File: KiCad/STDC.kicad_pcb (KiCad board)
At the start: 4 copper layers, 38 x 48 mm, 0 parts

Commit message: Use JLCPCB setup ported from Altium
https://gitlab.ethz.ch/villanif/altium_files/-/tree/master/example_design_rules
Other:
- rule pad_to_mask_clearance: 0 -> 0.075
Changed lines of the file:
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@@
 			(dielectric_constraints no)
 		)
-		(pad_to_mask_clearance 0)
+		(pad_to_mask_clearance 0.075)
 		(allow_soldermask_bridges_in_footprints no)
 		(tenting front back)

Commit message: First Draft PCB Layout
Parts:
- added C1: 4u7, Capacitor_SMD:C_0402_1005Metric, F.Cu at (149.1, 116.0)
- added C10: 15pF, Capacitor_SMD:C_0402_1005Metric, F.Cu at (137.8, 125.3)
- added C11: 100n, Capacitor_SMD:C_0402_1005Metric, F.Cu at (149.7, 103.3)
- added C12: 100n, Capacitor_SMD:C_0402_1005Metric, F.Cu at (135.8, 111.2)
- added C13: 100n, Capacitor_SMD:C_0402_1005Metric, F.Cu at (133.9, 118.1)
- added C14: 100n, Capacitor_SMD:C_0402_1005Metric, F.Cu at (136.6, 119.2)
- added C15: 100n, Capacitor_SMD:C_0402_1005Metric, F.Cu at (132.5, 126.8)
- added C16: 100n, Capacitor_SMD:C_0402_1005Metric, F.Cu at (126.1, 120.4)
- added C17: 100n, Capacitor_SMD:C_0402_1005Metric, F.Cu at (126.3, 118.6)
- added C18: 4u7, Capacitor_SMD:C_0402_1005Metric, F.Cu at (143.3, 109.3)
- added C19: 470n, Capacitor_SMD:C_0402_1005Metric, F.Cu at (138.9, 106.1)
- added C2: 4u7, Capacitor_SMD:C_0402_1005Metric, F.Cu at (149.1, 117.0)
- added C20: 22n, Capacitor_SMD:C_0402_1005Metric, F.Cu at (138.9, 107.1)
- added C21: 10n, Capacitor_SMD:C_0402_1005Metric, F.Cu at (138.9, 105.1)
- added C22: 220n, Capacitor_SMD:C_0402_1005Metric, F.Cu at (138.5, 104.1)
- added C23: 2n2, Capacitor_SMD:C_0402_1005Metric, F.Cu at (144.2, 101.4)
- added C24: 100p, Capacitor_SMD:C_0402_1005Metric, F.Cu at (144.2, 102.4)
- added C25: 10n, Capacitor_SMD:C_0402_1005Metric, F.Cu at (145.8, 104.4)
- added C26: 22n, Capacitor_SMD:C_0402_1005Metric, F.Cu at (145.8, 106.5)
- added C27: 470n, Capacitor_SMD:C_0402_1005Metric, F.Cu at (145.8, 105.4)
- added C28: 10u, Capacitor_SMD:C_0402_1005Metric, F.Cu at (147.7, 110.0)
- added C29: 10u, Capacitor_SMD:C_0402_1005Metric, F.Cu at (147.7, 111.1)
- added C3: 1u, Capacitor_SMD:C_0402_1005Metric, F.Cu at (137.3, 128.7)
- added C30: 100p, Capacitor_SMD:C_0402_1005Metric, F.Cu at (147.7, 112.2)
- added C31: 4u7, Capacitor_SMD:C_0402_1005Metric, F.Cu at (141.3, 111.8)
- added C32: 4u7, Capacitor_SMD:C_0402_1005Metric, F.Cu at (143.5, 116.7)
- added C33: 10u, Capacitor_SMD:C_0402_1005Metric, F.Cu at (143.5, 117.8)
- added C34: 10u, Capacitor_SMD:C_0402_1005Metric, F.Cu at (141.3, 110.8)
- added C35: 100p, Capacitor_SMD:C_0402_1005Metric, F.Cu at (128.7, 138.3)
- added C36: 10u, Capacitor_SMD:C_0402_1005Metric, F.Cu at (136.9, 135.0)
- added C37: 100n, Capacitor_SMD:C_0402_1005Metric, F.Cu at (133.5, 142.8)
- added C38: 1u, Capacitor_SMD:C_0402_1005Metric, F.Cu at (133.6, 139.8)
- added C39: 1u, Capacitor_SMD:C_0402_1005Metric, F.Cu at (133.4, 140.8)
- added C4: 10n, Capacitor_SMD:C_0402_1005Metric, F.Cu at (138.3, 128.7)
- added C40: 10u, Capacitor_SMD:C_0402_1005Metric, F.Cu at (133.5, 141.8)
- added C41: 1u, Capacitor_SMD:C_0402_1005Metric, F.Cu at (132.2, 132.7)
- added C42: 22u, Capacitor_SMD:C_0402_1005Metric, F.Cu at (132.2, 133.8)
- added C43: 100n, Capacitor_SMD:C_0402_1005Metric, F.Cu at (131.0, 142.7)
- added C44: 100n, Capacitor_SMD:C_0402_1005Metric, F.Cu at (136.3, 142.3)
- added C45: 100n, Capacitor_SMD:C_0402_1005Metric, F.Cu at (135.3, 142.3)
- added C46: 1u, Capacitor_SMD:C_0402_1005Metric, F.Cu at (135.6, 140.6)
- added C47: 4u7, Capacitor_SMD:C_0402_1005Metric, F.Cu at (128.5, 141.8)
- added C48: 4u7, Capacitor_SMD:C_0402_1005Metric, F.Cu at (130.0, 140.6)
- added C49: 100n, Capacitor_SMD:C_0402_1005Metric, F.Cu at (145.0, 142.8)
- added C5: 100n, Capacitor_SMD:C_0402_1005Metric, F.Cu at (142.1, 119.7)
- added C50: 100n, Capacitor_SMD:C_0402_1005Metric, F.Cu at (128.7, 142.8)
- added C51: 100n, Capacitor_SMD:C_0402_1005Metric, F.Cu at (153.8, 109.3)
- added C52: 100n, Capacitor_SMD:C_0402_1005Metric, F.Cu at (159.3, 111.4)
- added C53: 100n, Capacitor_SMD:C_0402_1005Metric, F.Cu at (162.0, 104.5)
- added C54: 100n, Capacitor_SMD:C_0402_1005Metric, F.Cu at (159.8, 101.7)
- added C55: 100n, Capacitor_SMD:C_0402_1005Metric, F.Cu at (151.5, 105.8)
- added C56: 100n, Capacitor_SMD:C_0402_1005Metric, F.Cu at (142.8, 141.3)
- added C57: 100n, Capacitor_SMD:C_0402_1005Metric, F.Cu at (148.6, 135.3)
- added C58: 100n, Capacitor_SMD:C_0402_1005Metric, F.Cu at (154.8, 144.0)
- added C59: 100n, Capacitor_SMD:C_0402_1005Metric, F.Cu at (158.8, 147.1)
- added C6: 100n, Capacitor_SMD:C_0402_1005Metric, F.Cu at (142.1, 134.2)
- added C60: 100n, Capacitor_SMD:C_0402_1005Metric, F.Cu at (158.6, 125.2)
- added C7: 100n, Capacitor_SMD:C_0402_1005Metric, F.Cu at (149.2, 134.2)
- added C8: 100n, Capacitor_SMD:C_0402_1005Metric, F.Cu at (139.3, 121.8)
- added C9: 15pF, Capacitor_SMD:C_0402_1005Metric, F.Cu at (137.8, 123.3)
- added D1: Orange, LED_SMD:LED_0603_1608Metric, F.Cu at (136.6, 101.6)
- added D2: Red, LED_SMD:LED_0603_1608Metric, F.Cu at (161.8, 121.0)
- added D3: Blue, LED_SMD:LED_0603_1608Metric, F.Cu at (161.8, 117.9)
- added D4: Green, LED_SMD:LED_0603_1608Metric, F.Cu at (153.1, 146.7)
- added IC1: BQ26221PW, TI-BQ26221PW:SOP65P640X120-8N, F.Cu at (130.9, 121.0)
- added IC2: R1200N001A-TR-FE, LIB_R1200N001A-TR-FE:SOT95P280X110-6N, F.Cu at (129.0, 133.8)
- added IC3: MS5849-30BA, MS5849-30BA:MS584930BA, F.Cu at (158.7, 104.9)
- added IC4: W25Q32JWSNIQ, Winbond-W25Q32JWSNIQ:SOIC127P600X175-8N, F.Cu at (156.3, 128.5)
- added J1: TC2030, Connector:Tag-Connect_TC2030-IDC-NL_2x03_P1.27mm_Vertical, F.Cu at (155.6, 115.2)
- added J2: Conn_01x03_BATT, Connector_JST:JST_PH_S3B-PH-K_1x03_P2.00mm_Horizontal, F.Cu at (128.2, 102.5)
- added J3: Conn_01x34_NHD_18, Connector_FFC-FPC:TE_3-1734839-4_1x34-1MP_P0.5mm_Horizontal, F.Cu at (137.5, 145.8)
- added L1: WPC Charging RX, L_IWAS4832-QiCoil:L_IWAS4832ABEB110JF1, F.Cu at (143.0, 103.3)
- added L2: 4u7, Inductor_SMD:L_1210_3225Metric, F.Cu at (138.5, 112.5)
- added L3: 2u2, Inductor_SMD:L_1210_3225Metric, F.Cu at (146.5, 115.2)
- added L4: 10u, Inductor_SMD:L_1812_4532Metric, F.Cu at (129.4, 130.0)
- added Q1: AO3400A, Package_TO_SOT_SMD:SOT-23, F.Cu at (127.5, 111.4)
- added Q2: AO3400A, Package_TO_SOT_SMD:SOT-23, F.Cu at (127.5, 115.4)
- added Q3: DMG2302U, Package_TO_SOT_SMD:SOT-23, F.Cu at (139.3, 134.7)
- added Q4: DMG2302U, Package_TO_SOT_SMD:SOT-23, F.Cu at (134.5, 130.6)
- added R1: 10k, Resistor_SMD:R_0402_1005Metric, F.Cu at (137.0, 126.9)
- added R10: 100k, Resistor_SMD:R_0402_1005Metric, F.Cu at (137.7, 119.2)
- added R11: 20m, Resistor_SMD:R_0402_1005Metric, F.Cu at (137.2, 117.7)
- added R12: 680R, Resistor_SMD:R_0402_1005Metric, F.Cu at (135.8, 108.5)
- added R13: 150R, Resistor_SMD:R_0402_1005Metric, F.Cu at (145.7, 107.8)
- added R14: 220R, Resistor_SMD:R_0402_1005Metric, F.Cu at (147.7, 108.9)
- added R15: 2k2, Resistor_SMD:R_0402_1005Metric, F.Cu at (141.4, 109.3)
- added R16: 680R, Resistor_SMD:R_0402_1005Metric, F.Cu at (159.5, 120.1)
- added R17: 150R, Resistor_SMD:R_0402_1005Metric, F.Cu at (159.5, 118.9)
- added R18: 100k, Resistor_SMD:R_0402_1005Metric, F.Cu at (128.2, 136.8)
- added R19: 200k, Resistor_SMD:R_0402_1005Metric, F.Cu at (129.3, 136.8)
- added R2: 10k, Resistor_SMD:R_0402_1005Metric, F.Cu at (143.9, 119.3)
- added R20: 220k, Resistor_SMD:R_0402_1005Metric, F.Cu at (132.2, 134.9)
- added R21: 15k, Resistor_SMD:R_0402_1005Metric, F.Cu at (126.3, 134.0)
- added R22: 49.9R, Resistor_SMD:R_0402_1005Metric, F.Cu at (131.7, 139.2)
- added R23: 10k, Resistor_SMD:R_0402_1005Metric, F.Cu at (138.7, 140.0)
- added R24: 10k, Resistor_SMD:R_0402_1005Metric, F.Cu at (139.2, 138.6)
- added R25: 1M5, Resistor_SMD:R_0402_1005Metric, F.Cu at (143.0, 142.8)
- added R26: 2k2, Resistor_SMD:R_0402_1005Metric, F.Cu at (159.2, 108.5)
- added R27: 2k2, Resistor_SMD:R_0402_1005Metric, F.Cu at (161.1, 108.5)
- added R28: 2k2, Resistor_SMD:R_0402_1005Metric, F.Cu at (159.1, 112.8)
- added R29: 2k2, Resistor_SMD:R_0402_1005Metric, F.Cu at (159.1, 114.2)
- added R3: 150R, Resistor_SMD:R_0402_1005Metric, F.Cu at (134.8, 114.6)
- added R30: 10k, Resistor_SMD:R_0402_1005Metric, F.Cu at (149.7, 139.0)
- added R31: 10k, Resistor_SMD:R_0402_1005Metric, F.Cu at (149.8, 144.9)
- added R32: 10k, Resistor_SMD:R_0402_1005Metric, F.Cu at (151.3, 145.4)
- added R33: 680R, Resistor_SMD:R_0402_1005Metric, F.Cu at (154.5, 147.1)
- added R34: 10k, Resistor_SMD:R_0402_1005Metric, F.Cu at (152.1, 131.9)
- added R35: 10k, Resistor_SMD:R_0402_1005Metric, F.Cu at (160.7, 127.0)
- added R36: 10k, Resistor_SMD:R_0402_1005Metric, F.Cu at (161.2, 129.2)
- added R4: 10k, Resistor_SMD:R_0402_1005Metric, F.Cu at (127.2, 126.7)
- added R5: 10k, Resistor_SMD:R_0402_1005Metric, F.Cu at (132.7, 124.8)
- added R6: 10k, Resistor_SMD:R_0402_1005Metric, F.Cu at (127.6, 123.4)
- added R7: 1k, Resistor_SMD:R_0402_1005Metric, F.Cu at (130.4, 112.4)
- added R8: 10k, Resistor_SMD:R_0402_1005Metric, F.Cu at (131.1, 118.4)
- added R9: 100k, Resistor_SMD:R_0402_1005Metric, F.Cu at (132.7, 118.1)
- added TP1: TestPoint, TestPoint:TestPoint_THTPad_1.0x1.0mm_Drill0.5mm, F.Cu at (149.0, 101.8)
- added TP2: UART_TX, TestPoint:TestPoint_THTPad_1.0x1.0mm_Drill0.5mm, F.Cu at (151.0, 101.8)
- added TP3: UART_RX, TestPoint:TestPoint_THTPad_1.0x1.0mm_Drill0.5mm, F.Cu at (153.0, 101.8)
- added TP4: TestPoint, TestPoint:TestPoint_THTPad_1.0x1.0mm_Drill0.5mm, F.Cu at (155.0, 101.8)
- added U1: STM32L476RGTx, Package_QFP:LQFP-64_10x10mm_P0.5mm, F.Cu at (145.6, 127.0)
- added U10: SN74LV1T34DCK, Package_TO_SOT_SMD:SOT-353_SC-70-5, F.Cu at (144.7, 139.2)
- added U11: SN74LV1T34DCK, Package_TO_SOT_SMD:SOT-353_SC-70-5, F.Cu at (145.7, 136.6)
- added U12: RN4871, RF_Module:Microchip_RN4871, F.Cu at (154.3, 138.1)
- added U13: LM810, Package_TO_SOT_SMD:SOT-23, F.Cu at (148.4, 141.3)
- added U14: SN74LV1T34DCK, Package_TO_SOT_SMD:SOT-353_SC-70-5, F.Cu at (158.3, 145.2)
- added U2: DW01A, Package_TO_SOT_SMD:SOT-23-6, F.Cu at (133.2, 111.9)
- added U3: TXS0101DBV, Package_TO_SOT_SMD:SOT-23-6, F.Cu at (129.8, 126.2)
- added U4: BQ51050BRHL, Package_DFN_QFN:Texas_VQFN-RHL-20, F.Cu at (142.5, 106.0)
- added U5: PAM2306AYPKE, Package_DFN_QFN:WDFN-12-1EP_3x3mm_P0.45mm_EP1.7x2.5mm, F.Cu at (142.3, 114.2)
- added U6: MCP1700x-250xxTT, Package_TO_SOT_SMD:SOT-23, F.Cu at (135.8, 136.9)
- added U7: SN74LV1T34DCK, Package_TO_SOT_SMD:SOT-353_SC-70-5, F.Cu at (155.7, 109.6)
- added U8: SN74LV1T34DCK, Package_TO_SOT_SMD:SOT-353_SC-70-5, F.Cu at (153.9, 105.5)
- added U9: PCA9306, Package_SON:X2SON-8_1.4x1mm_P0.35mm, F.Cu at (159.7, 109.9)
- added X1: Q13FC1350000400, Crystal:Crystal_SMD_3215-2Pin_3.2x1.5mm, F.Cu at (136.1, 124.3)
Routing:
- net DISPLAY_VCC: track 0.00 -> 19.9 mm
- net /Display/VCOMH: track 0.00 -> 16.9 mm
- added copper zone on B.Cu, net GND
- added copper zone on In1.Cu, net GND

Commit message: Implement Comments, Working on PCB Layout
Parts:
- removed the C15 at (132.5, 126.8)
- removed the C16 at (126.1, 120.4)
- removed the C17 at (126.3, 118.6)
- removed the C38 at (133.6, 139.8)
- removed Q3, Q4: DMG2302U, Package_TO_SOT_SMD:SOT-23
- removed the R10 at (137.7, 119.2)
- removed the R11 at (137.2, 117.7)
- removed the R4 at (127.2, 126.7)
- removed the R6 at (127.6, 123.4)
- removed the R8 at (131.1, 118.4)
- removed the R9 at (132.7, 118.1)
- added C37: 100n, Capacitor_SMD:C_0402_1005Metric, F.Cu at (137.5, 137.2)
- added D4: RB522ES-30T15R, RB522ES-30T15R:RB522ES30, F.Cu at (134.3, 135.0)
- added D5: RB522ES-30T15R, RB522ES-30T15R:RB522ES30, F.Cu at (132.5, 135.0)
- added IC2: TPS22916CNYFPR, TPS22916CNYFPR:BGA4C40P2X2_78X78X50, F.Cu at (133.8, 128.1)
- IC1: value BQ26221PW -> TPS22916CNYFPR; footprint TI-BQ26221PW:SOP65P640X120-8N -> TPS22916CNYFPR:BGA4C40P2X2_78X78X50
- U3: value TXS0101DBV -> MAX17262REWL_T; footprint Package_TO_SOT_SMD:SOT-23-6 -> MAX17262REWL_T:BGA9N40P3X3_144X146X69N
- moved IC1 16.1 mm to (140.2, 134.1)
- moved R28 9.98 mm to (158.8, 124.5)
- moved U3 7.63 mm to (132.3, 119.0), turned to 90 degrees
- moved R29 7.07 mm to (154.5, 130.4), turned to 90 degrees
- moved R30 6.84 mm to (154.4, 128.2), turned to -90 degrees
- moved C57 6.39 mm to (156.4, 131.2), turned to 0 degrees
- moved J2 6.17 mm to (132.0, 107.4), turned to 180 degrees
- moved J1 6.16 mm to (155.1, 121.4)
- moved R5 5.97 mm to (129.6, 119.7), turned to 0 degrees
- moved C30 5.05 mm to (148.5, 118.5), turned to 0 degrees
- moved R6 4.51 mm to (136.1, 104.0), turned to -90 degrees
- moved C38 4.04 mm to (136.0, 137.7), turned to 90 degrees
- moved C13 3.85 mm to (130.1, 118.2), turned to -90 degrees
- moved C48 3.53 mm to (153.6, 112.8)
- moved U7 3.53 mm to (155.4, 113.1)
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- renumbered C18 to C15, C19 to C16, C20 to C17, C21 to C18, C22 to C19, C23 to C20, C24 to C21, C25 to C22, C26 to C23, C27 to C24, C28 to C25, C29 to C26, C30 to C27, C31 to C28, C32 to C29, C33 to C30, C34 to C31, C35 to C32, C41 to C33, C42 to C34, C36 to C35, C37 to C36, C39 to C38, C40 to C39, C43 to C40, C44 to C41, C45 to C42, C46 to C43, C47 to C44, C48 to C45, C49 to C46, C50 to C47, C51 to C48, C52 to C49, C53 to C50, C54 to C51, C55 to C52, C56 to C53, C57 to C54, C58 to C55, C59 to C56, C60 to C57, D4 to D6, IC2 to IC3, IC3 to IC4, IC4 to IC5, R16 to R10, R17 to R11, R18 to R12, R19 to R13, R20 to R14, R21 to R15, R22 to R16, R23 to R17, R24 to R18, R25 to R19, R26 to R20, R27 to R21, R28 to R22, R29 to R23, R30 to R24, R31 to R25, R32 to R26, R33 to R27, R34 to R28, R35 to R29, R36 to R30, R7 to R4, R12 to R6, R13 to R7, R14 to R8, R15 to R9
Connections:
- C13 pad 1: /Power+Battery/BAT_STAT_SRP -> /Power+Battery/BATT+
- C13 pad 2: /Power+Battery/BATT- -> GND
- C14 pad 1: /Power+Battery/BAT_STAT_SRN -> /Power+Battery/Stat_REG
- C14 pad 2: /Power+Battery/BATT- -> GND
- C15 pad 1: BATTERY_PWR -> /Power+Battery/BATT+
- C28 pad 1: BATTERY_PWR -> SYS_PWR
- C29 pad 1: BATTERY_PWR -> SYS_PWR
- D1 pad 2: BATTERY_PWR -> /Power+Battery/BATT+
- J2 pad 3: BATTERY_PWR -> /Power+Battery/BATT+
- R3 pad 1: BATTERY_PWR -> /Power+Battery/BATT+
- R5 pad 1: +1V8 -> /Power+Battery/TS_CTRL
- R5 pad 2: /BAT_STATUS_HDQ -> /Power+Battery/TS_CTRL_R
- U1 pad 8: unconnected-(U1-PC0-Pad8) -> /Power+Battery/Batt_Status_SCL
- U1 pad 9: /BAT_STATUS_HDQ -> /Power+Battery/Batt_Status_SDA
- U4 pad 11: BATTERY_PWR -> /Power+Battery/BATT+
- U4 pad 4: BATTERY_PWR -> /Power+Battery/BATT+
- U5 pad 1: BATTERY_PWR -> SYS_PWR
- U5 pad 12: BATTERY_PWR -> SYS_PWR
- U5 pad 6: BATTERY_PWR -> SYS_PWR
- U5 pad 7: BATTERY_PWR -> SYS_PWR
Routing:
- net GND: track 0.00 -> 52.8 mm, vias 0 -> 45
- net +1V8: track 0.00 -> 46.5 mm
- net /Power+Battery/TS_CTRL: track 0.00 -> 42.0 mm, vias 0 -> 2
- net +3.3V: track 0.00 -> 27.0 mm
- net //Display_SPI_CS: track 0.00 -> 15.6 mm
- net /Power+Battery/Batt_Status_SDA: track 0.00 -> 13.6 mm, vias 0 -> 2
- net /Power+Battery/Batt_Status_SCL: track 0.00 -> 13.1 mm
- net /SPI_MISO: track 0.00 -> 12.1 mm
- net /SPI_NSS: track 0.00 -> 10.8 mm, vias 0 -> 2
- net /Power+Battery/AC1: track 0.00 -> 9.96 mm
- net /Power+Battery//CHARGE: track 0.00 -> 7.97 mm
- net /Display/VSL: track 0.00 -> 7.76 mm
- net DISPLAY_VCI: track 0.00 -> 7.69 mm
- net /Power+Battery/OC: track 0.00 -> 7.26 mm
- net DISPLAY_VCC: track 19.9 -> 26.8 mm
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- added copper zone on F.Cu, net /Display/17V_VFB
- added copper zone on F.Cu, net /Display/LX4
- added copper zone on F.Cu, net /Power+Battery/BATT+
- added copper zone on F.Cu, net /Power+Battery/FOD
- added copper zone on F.Cu, net DISPLAY_BATT_PWR
- added copper zone on F.Cu, net DISPLAY_VCC
- added copper zone on F.Cu, net DISPLAY_VCI
- added copper zone on F.Cu, net GND
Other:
- rule pad_to_mask_clearance: 0.075 -> 0.05

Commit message: PCB Layout V0.1 with errors
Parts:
- moved C2 11.7 mm to (137.4, 113.9), turned to -90 degrees
- moved C1 10.4 mm to (138.4, 113.9), turned to -90 degrees
- moved C30 6.25 mm to (142.6, 116.5), turned to 180 degrees
- moved D2 3.15 mm to (161.8, 117.8), turned to -90 degrees
- moved D3 3.09 mm to (161.8, 121.0), turned to 90 degrees
- moved C29 3.06 mm to (142.6, 115.3)
- moved C28 2.89 mm to (140.5, 110.6), turned to 0 degrees
- moved U5 2.61 mm to (141.6, 113.0)
- moved L2 2.38 mm to (137.6, 110.7)
- moved C31 2.30 mm to (140.5, 109.3)
- moved R28 1.29 mm to (160.1, 124.5)
- moved R10 1.20 mm to (159.9, 119.3)
- moved R11 1.15 mm to (159.9, 120.5)
- moved R29 0.72 mm to (154.0, 129.9), turned to 0 degrees
- moved L3 0.66 mm to (145.7, 115.5)
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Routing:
- net +1V8: track 46.5 -> 148.9 mm, vias 0 -> 5
- net +3.3V: track 27.0 -> 103.0 mm, vias 0 -> 3
- net /Power+Battery/BATT+: track 4.46 -> 60.6 mm, vias 0 -> 4
- net /Debug_UART_TX: track 0.00 -> 33.2 mm, vias 0 -> 1
- net /Debug_UART_RX: track 0.00 -> 32.9 mm, vias 0 -> 1
- net GND: track 52.8 -> 78.9 mm, vias 45 -> 87
- net /BLE_TX_IND: track 0.00 -> 25.7 mm, vias 0 -> 2
- net /Pressure Sensor/I2C_SDA: track 0.09 -> 23.2 mm, vias 0 -> 2
- net /Pressure Sensor/I2C_SCL: track 0.00 -> 21.6 mm, vias 0 -> 2
- net DISPLAY_EN: track 0.00 -> 18.7 mm, vias 0 -> 3
- net /Pressure Sensor/Pressure_INT: track 0.00 -> 18.5 mm, vias 0 -> 2
- net /Bluetooth Module/SYS_CONF: track 0.00 -> 18.2 mm
- net /DISPLAY_DATA_COMM: track 0.00 -> 17.2 mm, vias 0 -> 2
- net /DISPLAY_RST: track 0.00 -> 16.5 mm, vias 0 -> 2
- net /JTRST: track 0.00 -> 16.3 mm
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- added copper zone on F.Cu, net +1V8
- added copper zone on F.Cu, net +3.3V
- added copper zone on F.Cu, net /Power+Battery/AC2
- added copper zone on F.Cu, net /Power+Battery/BATT-
- added copper zone on F.Cu, net /Power+Battery/LX2
- added copper zone on F.Cu, net /Power+Battery/LX3
- added copper zone on F.Cu, net SYS_PWR
- added copper zone on In2.Cu, net SYS_PWR

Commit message: Fix almost all issues
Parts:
- moved R6 0.51 mm to (135.6, 104.1)
- moved R7 0.44 mm to (148.1, 108.3)
- moved C31 0.27 mm to (140.3, 109.5)
- moved C12 0.15 mm to (135.4, 112.5)
- moved C28 0.14 mm to (140.3, 110.6)
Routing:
- net /Power+Battery/BATT+: track 60.6 -> 9.06 mm, vias 4 -> 7
- net SYS_PWR: track 13.9 -> 1.13 mm, vias 8 -> 9
- net /Power+Battery//CHARGE: track 7.48 -> 8.70 mm, vias 2 -> 0
- net /Power+Battery/Batt_Status_SDA: track 13.9 -> 13.0 mm
- net +3.3V: track 103.0 -> 103.6 mm
- net /Power+Battery/Batt_Status_SCL: track 13.5 -> 13.1 mm, vias 2 -> 0
- net /Power+Battery/TS_CTRL: track 42.0 -> 42.3 mm, vias 2 -> 4
- added copper zone on In2.Cu, net /Power+Battery/BATT+

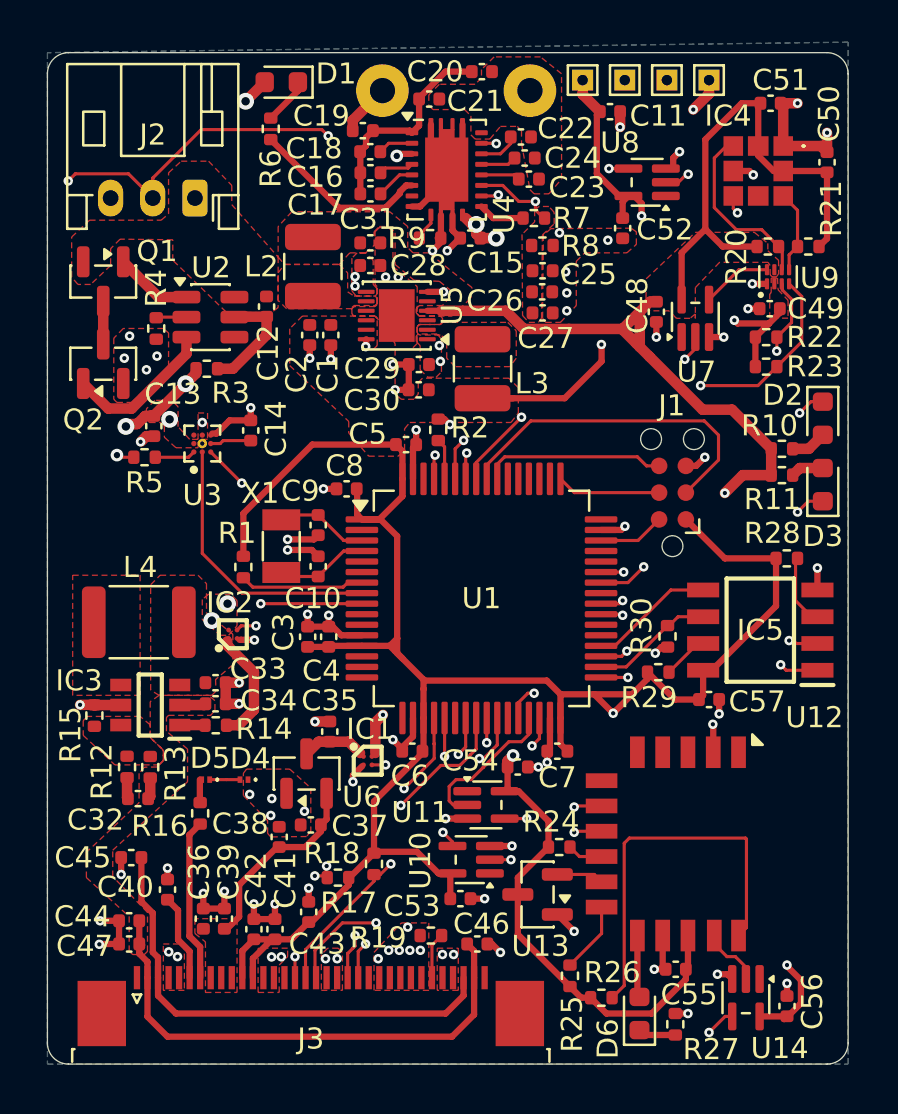
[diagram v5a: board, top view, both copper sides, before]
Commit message: Fix all except clearance violations
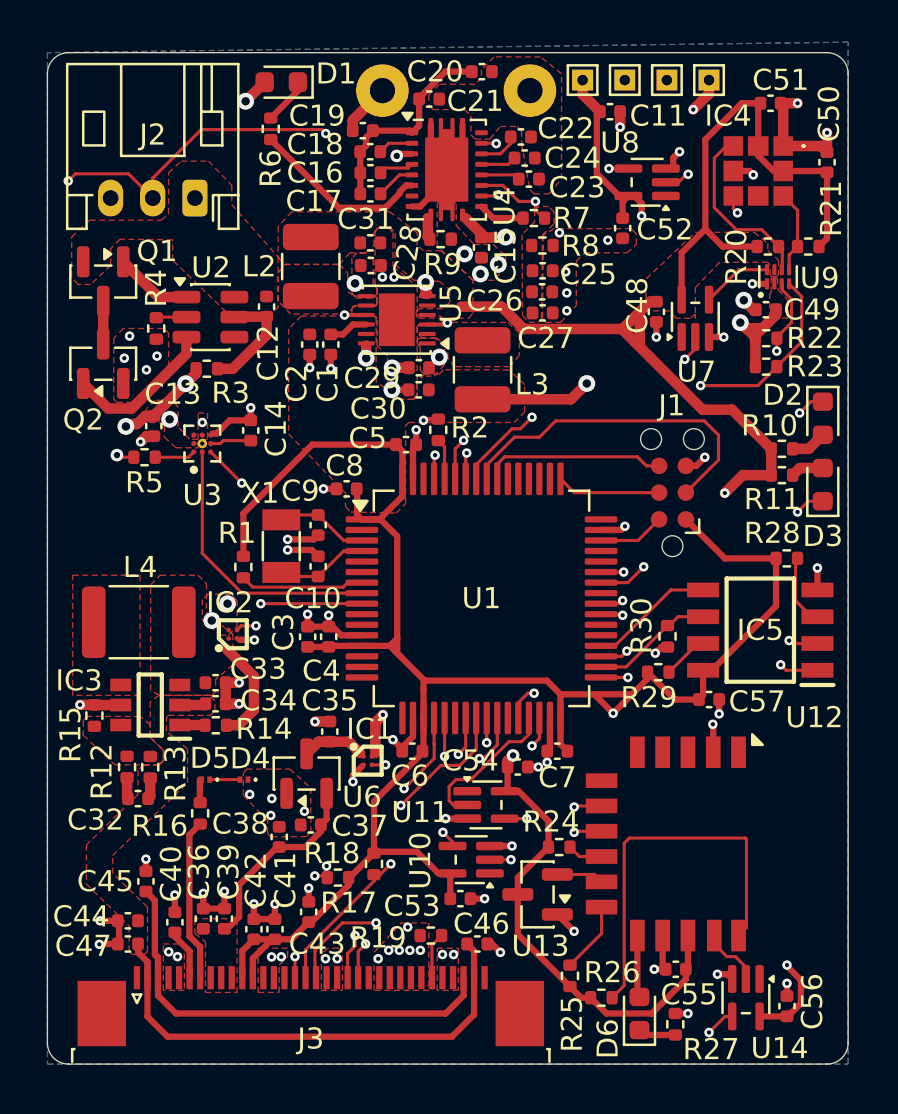
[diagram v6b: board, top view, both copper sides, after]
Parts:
- moved C40 1.59 mm to (131.1, 141.8)
- moved C45 1.33 mm to (129.7, 139.8), turned to 90 degrees
- moved C15 0.70 mm to (145.6, 109.8), turned to -90 degrees
- moved R9 0.50 mm to (143.7, 109.3)
- moved C1 0.45 mm to (138.4, 114.3)
- moved C2 0.45 mm to (137.4, 114.3)
- moved U5 0.20 mm to (141.6, 113.2)
- moved C49 0.19 mm to (159.1, 112.7)
- moved C29 0.15 mm to (142.6, 115.5)
- moved L2 0.10 mm to (137.5, 110.7)
- moved C44 0.06 mm to (128.8, 141.7)
- moved C47 0.06 mm to (128.8, 142.8)
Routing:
- net GND: track 78.8 -> 76.1 mm, vias 87 -> 90
- net +3.3V: track 103.6 -> 101.5 mm
- net /Display/VCOMH: track 22.9 -> 21.2 mm
- net /Display/VBREF: track 4.13 -> 2.44 mm
- net +1V8: track 148.9 -> 150.3 mm
- net DISPLAY_VCC: track 26.8 -> 25.7 mm
- net SYS_PWR: track 1.13 -> 1.23 mm, vias 9 -> 7
- net /Power+Battery/BATT+: vias 7 -> 6

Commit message: Some track spacing
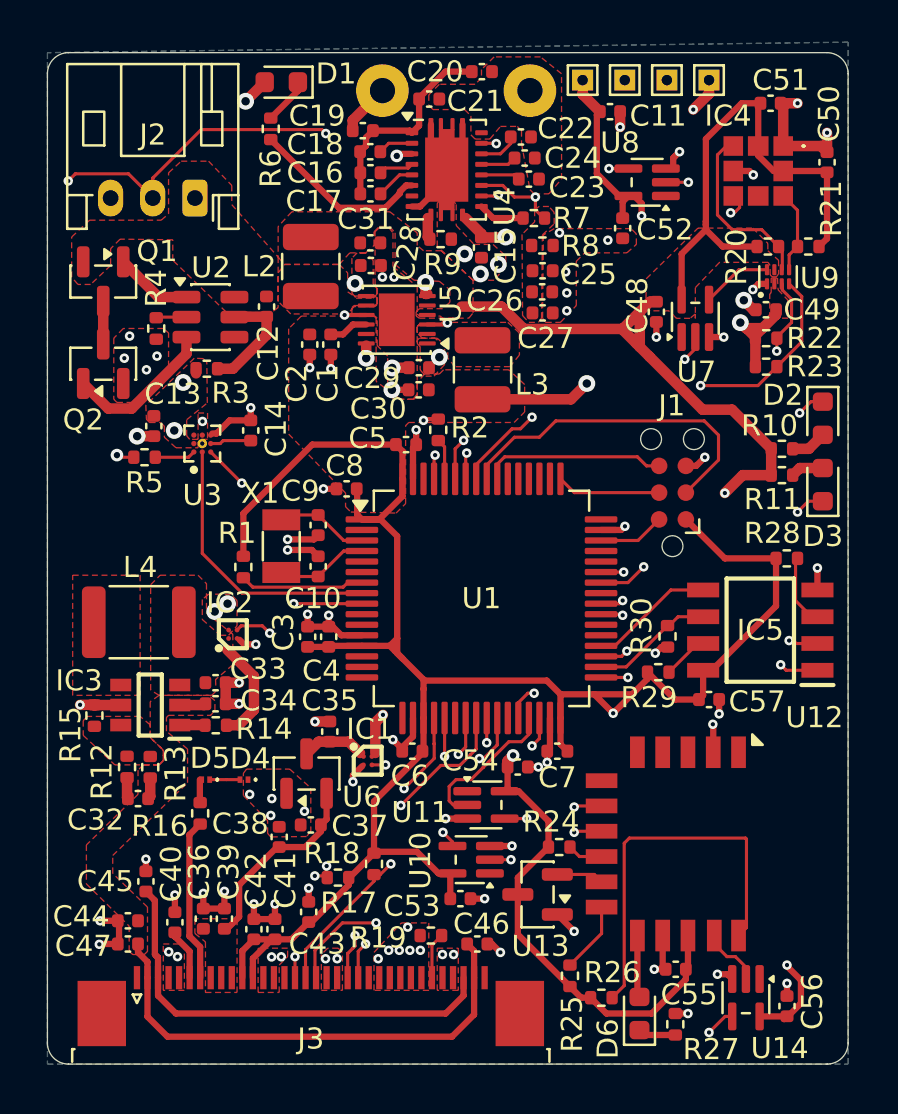
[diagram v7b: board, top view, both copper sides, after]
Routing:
- net /Power+Battery/BATT+: track 9.06 -> 4.67 mm, vias 6 -> 5
- net DISPLAY_EN: track 18.7 -> 19.5 mm
